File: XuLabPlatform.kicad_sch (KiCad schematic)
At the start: 11 parts, among them J10 Servo, J11 Servo, J12 Thruster, J15 I2C, J16 UART, J4 Servo, J5 Servo, J6 Servo, J7 Servo, J8 Servo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

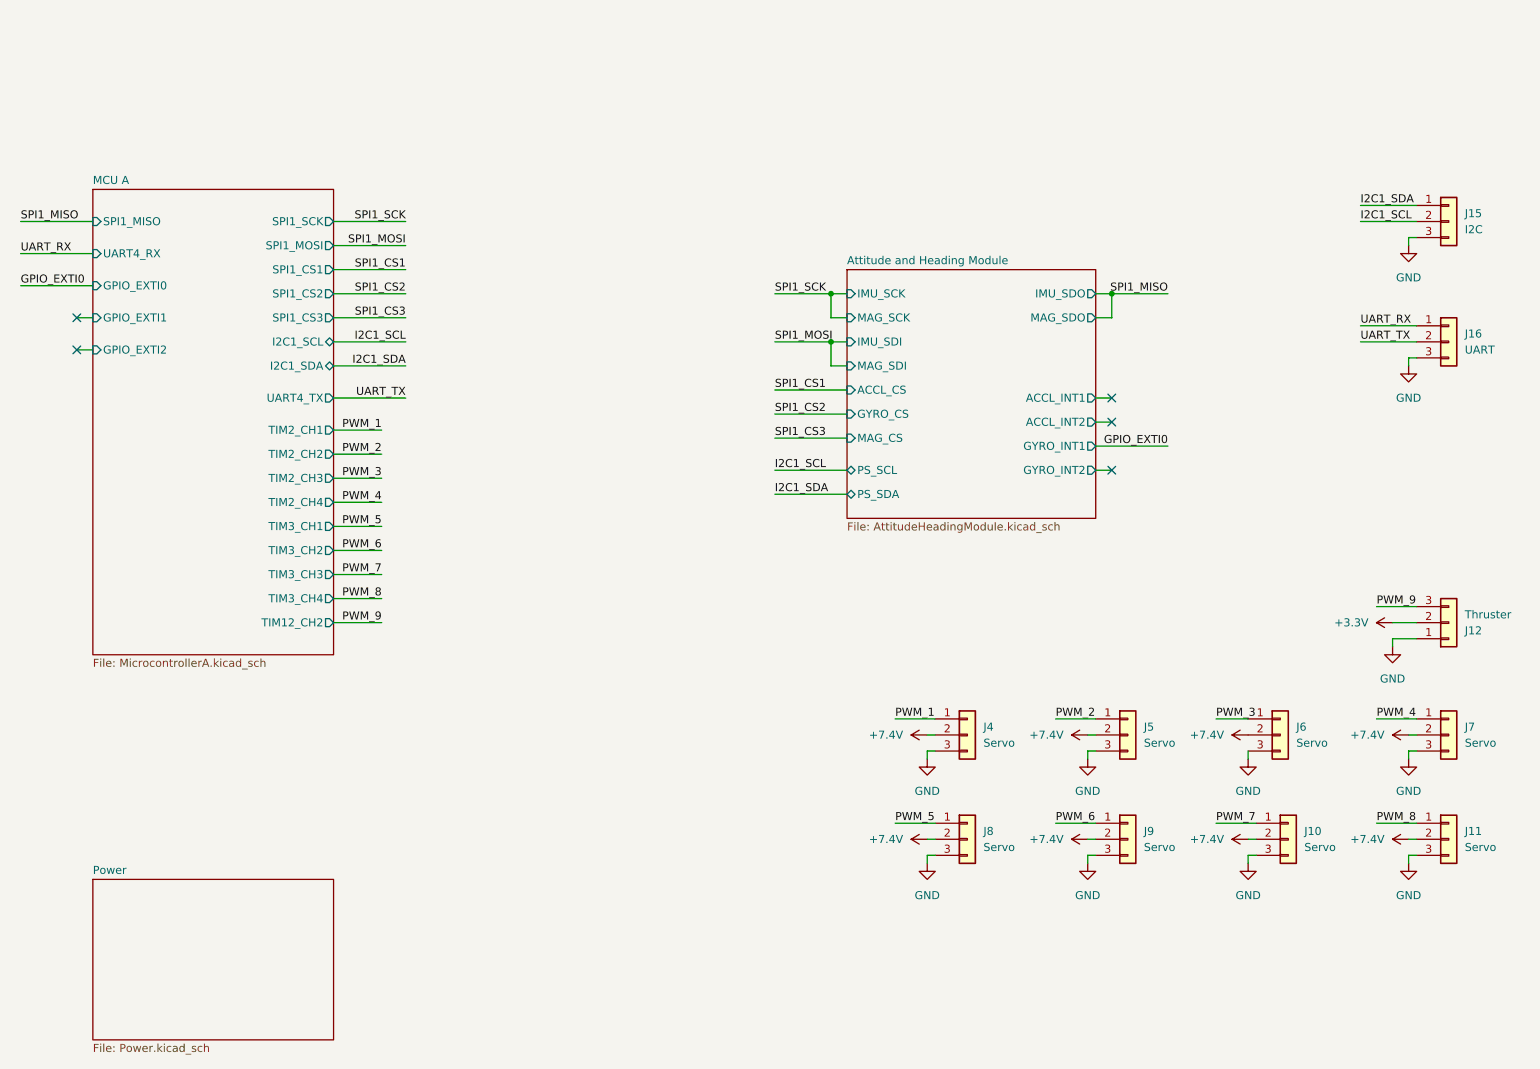
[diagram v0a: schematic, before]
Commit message: Add second SPI pins and connector
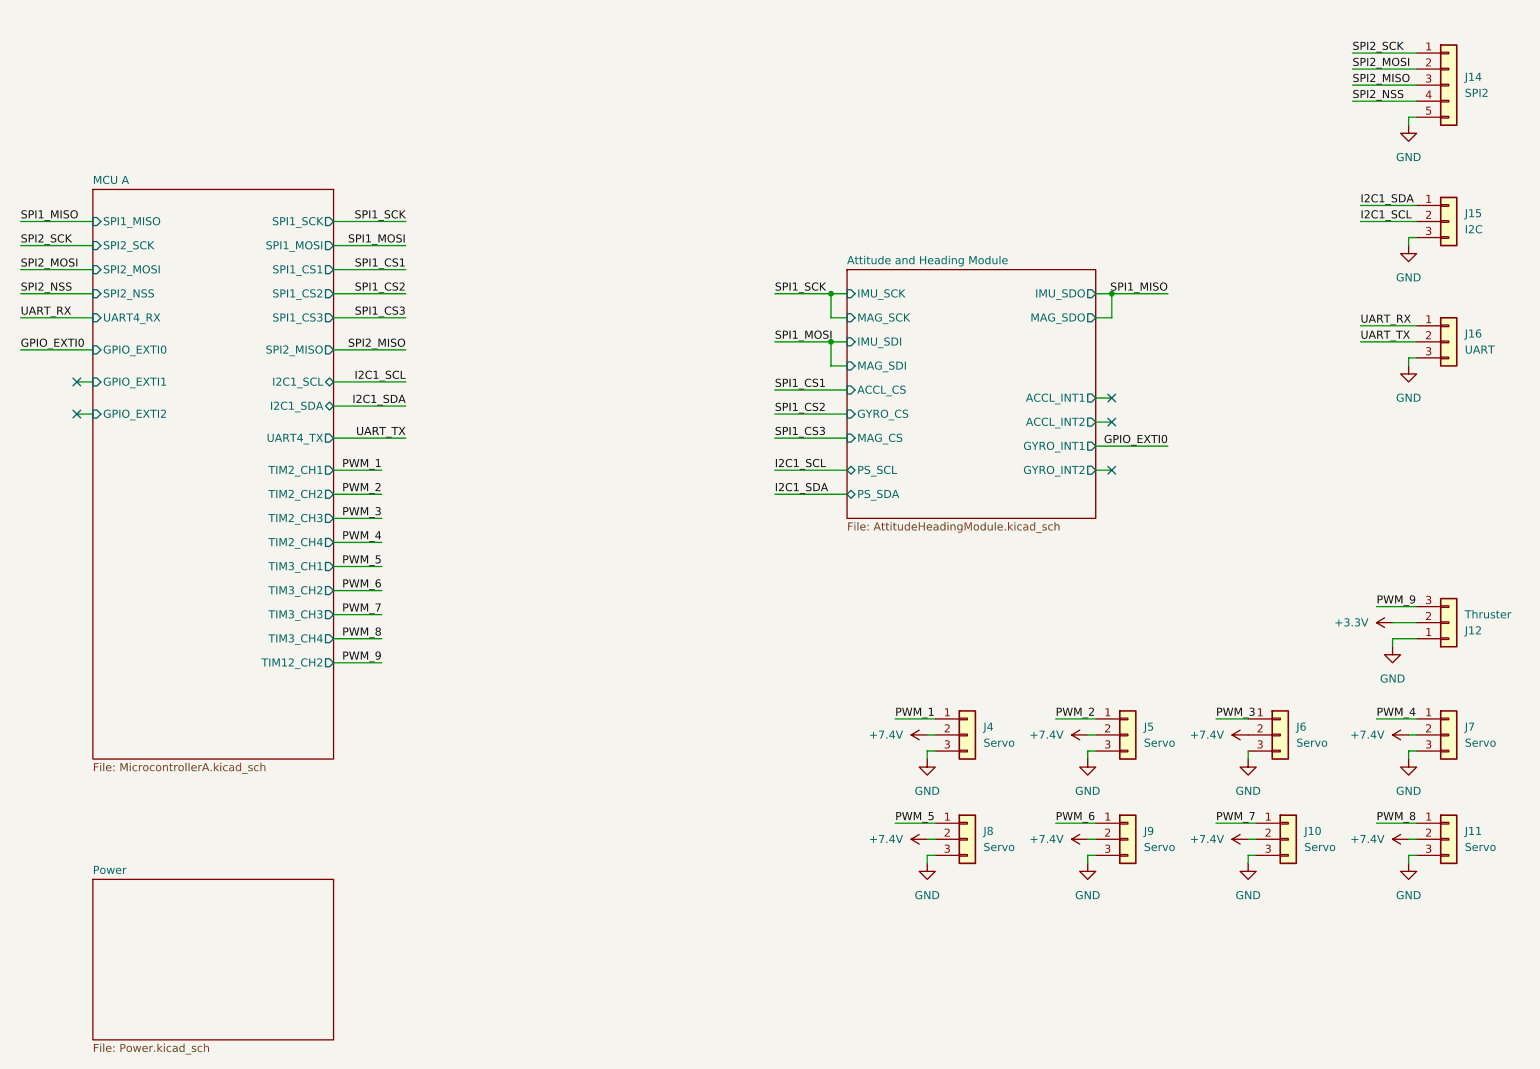
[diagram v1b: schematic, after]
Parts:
- added J14: SPI2, Connector_Molex:Molex_PicoBlade_53048-0510_1x05_P1.25mm_Horizontal, symbol Connector_Generic:Conn_01x05
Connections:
- net GND: now also J14.5 (Pin_5)
- new net SPI2_MISO: J14.3 (Pin_3)
- new net SPI2_MOSI: J14.2 (Pin_2)
- new net SPI2_NSS: J14.4 (Pin_4)
- new net SPI2_SCK: J14.1 (Pin_1)
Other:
- sheet MCU A ports: added SPI2_MISO, SPI2_MOSI, SPI2_NSS, SPI2_SCK; removed none

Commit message: Add second UART interface and connector
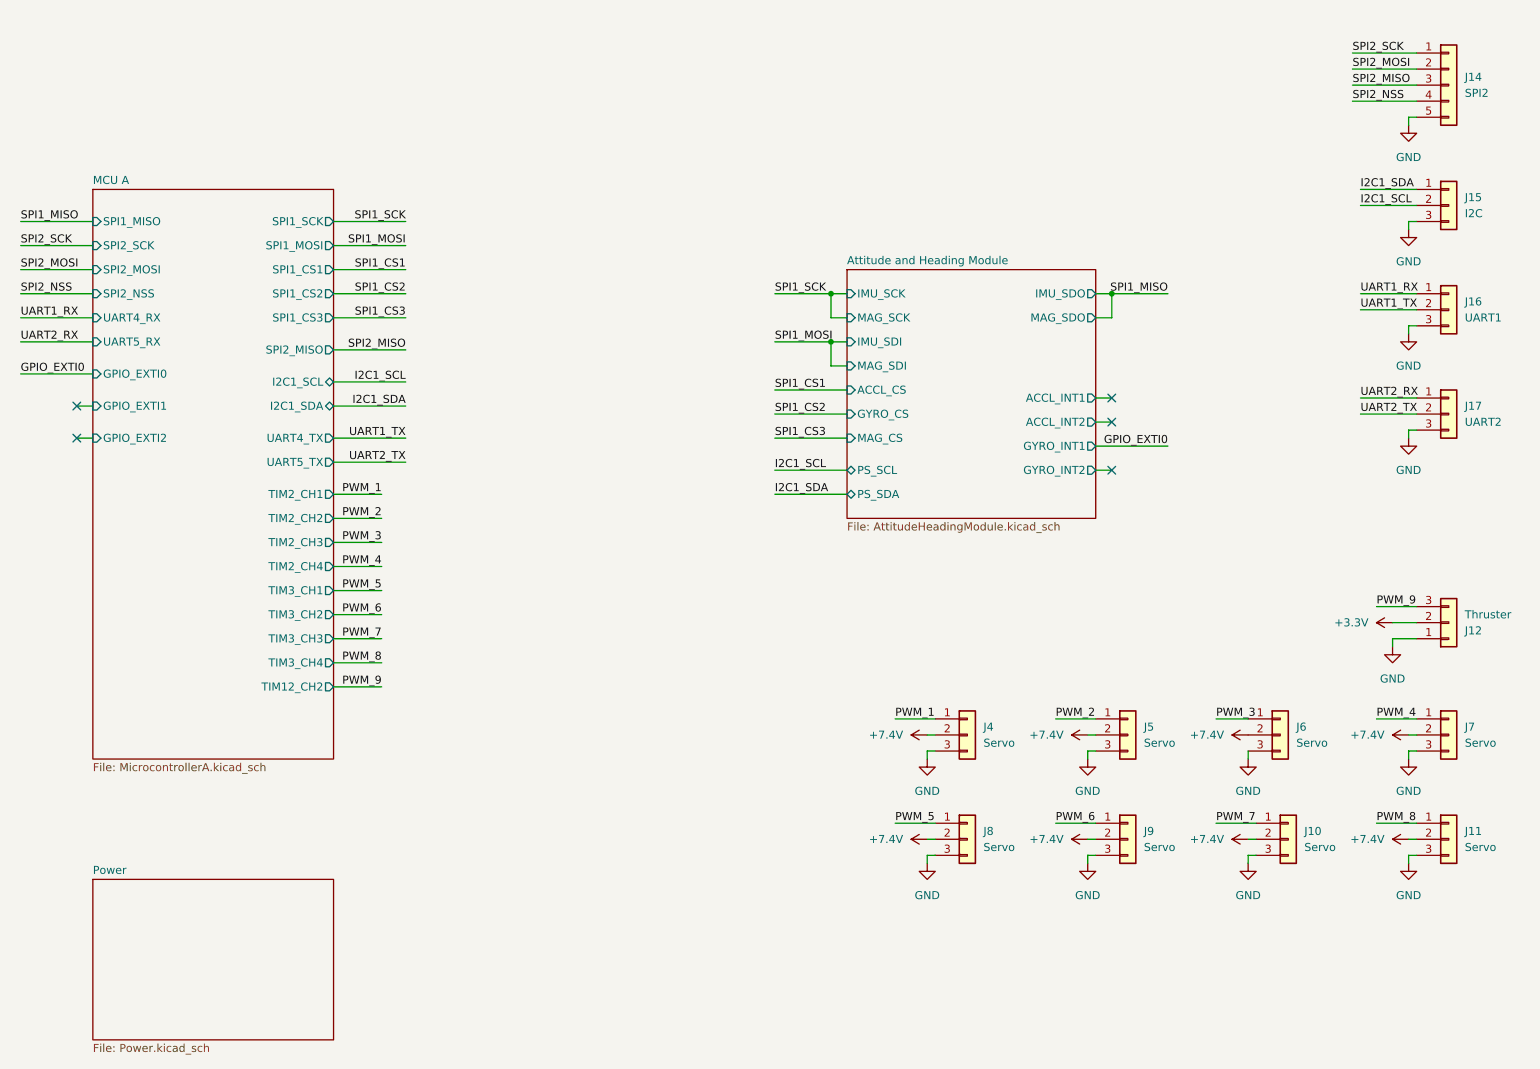
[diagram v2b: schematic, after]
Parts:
- added J17: UART2, Connector_Molex:Molex_PicoBlade_53048-0310_1x03_P1.25mm_Horizontal, symbol Connector_Generic:Conn_01x03
- J16: value UART -> UART1
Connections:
- net GND: now also J17.3 (Pin_3)
- net UART_RX renamed UART1_RX
- net UART_TX renamed UART1_TX
- new net UART2_RX: J17.1 (Pin_1)
- new net UART2_TX: J17.2 (Pin_2)
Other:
- sheet MCU A ports: added UART5_RX, UART5_TX; removed none
- moved on the sheet: J15, J16

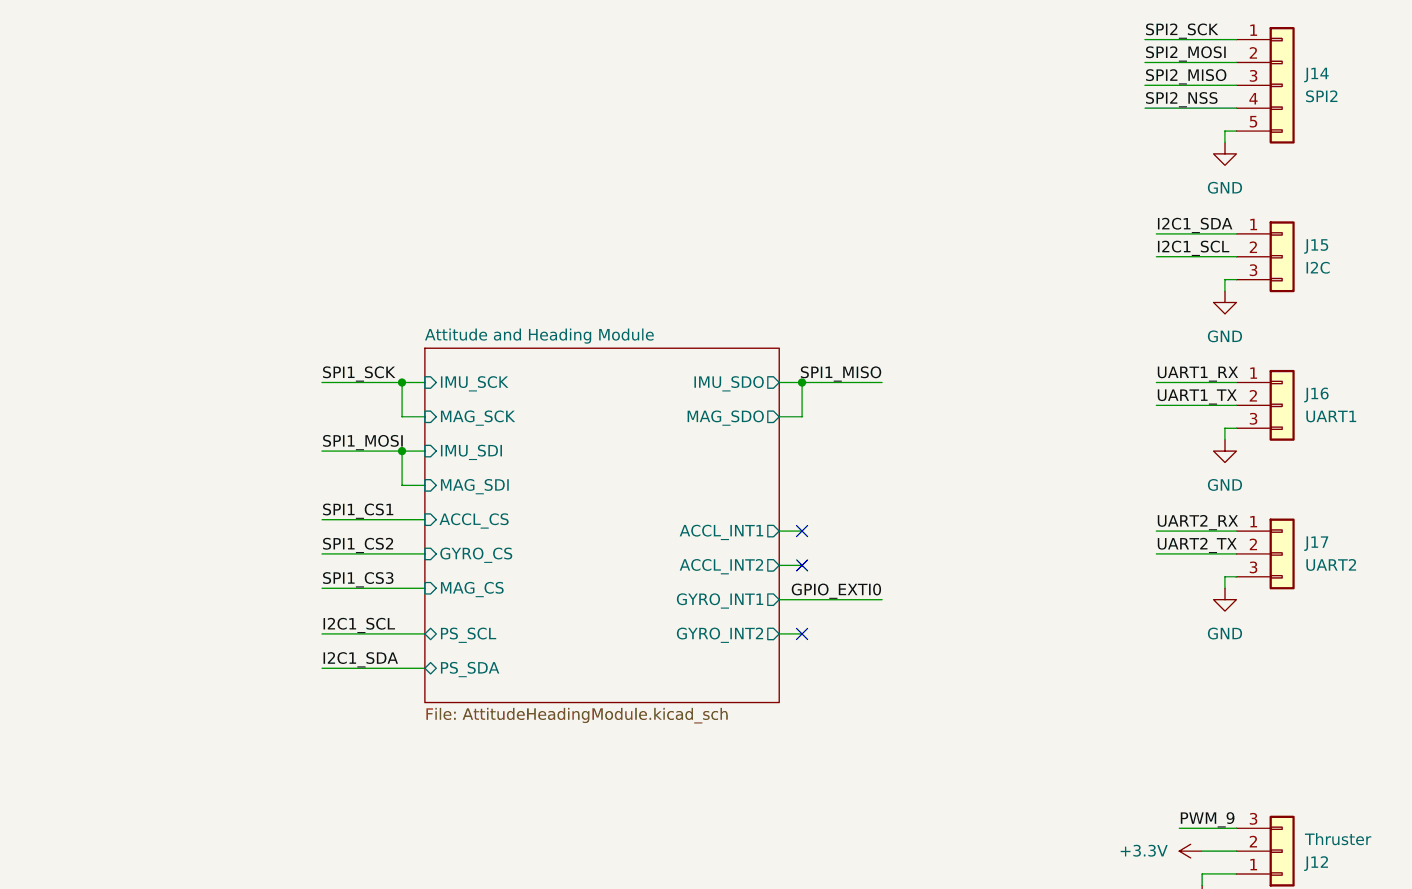
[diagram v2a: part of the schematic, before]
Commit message: Add second I2C connector
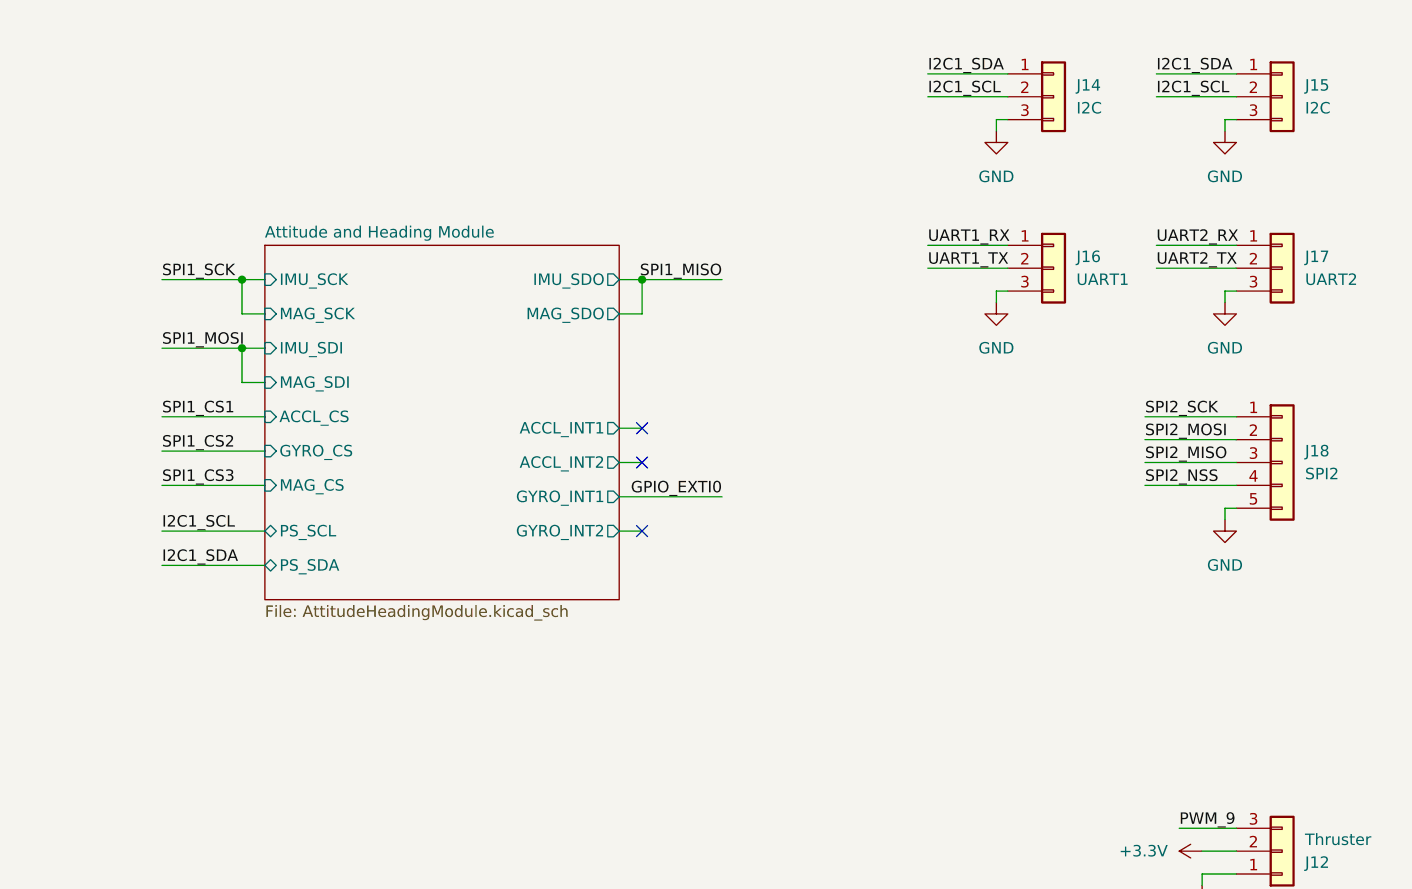
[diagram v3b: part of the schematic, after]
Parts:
- added J15: I2C, Connector_Molex:Molex_PicoBlade_53048-0310_1x03_P1.25mm_Horizontal, symbol Connector_Generic:Conn_01x03
- renumbered J15 to J14, J14 to J18
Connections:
- net GND: now also J15.3 (Pin_3)
- net I2C1_SCL: now also J15.2 (Pin_2)
- net I2C1_SDA: now also J15.1 (Pin_1)
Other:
- moved on the sheet: J14, J16, J17, J18

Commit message: Add second SPI1 connector
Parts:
- added J18: SPI1, Connector_Molex:Molex_PicoBlade_53048-0510_1x05_P1.25mm_Horizontal, symbol Connector_Generic:Conn_01x05
- renumbered J18 to J19
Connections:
- net GND: now also J18.5 (Pin_5)
- net SPI1_MISO: now also J18.3 (Pin_3)
- net SPI1_MOSI: now also J18.2 (Pin_2)
- net SPI1_SCK: now also J18.1 (Pin_1)
- new net SPI1_CS0: J18.4 (Pin_4)
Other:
- sheet MCU A ports: added SPI1_CS0; removed none

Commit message: Connect MCU interrupt pins to sensors
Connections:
- no-connect marks 5 -> 2
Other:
- sheet Attitude and Heading Module ports: added MAG_INT; removed none
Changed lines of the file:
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@@
 	)
 	(no_connect
-		(at 48.26 77.47)
-	)
-	(no_connect
-		(at 48.26 82.55)
-	)
-	(no_connect
-		(at 194.31 64.77)
-	)
-	(no_connect
 		(at 194.31 68.58)
 	)
@@
 	(wire
 		(pts
-			(xy 48.26 77.47) (xy 50.8 77.47)
-		)
-		(stroke
-			(width 0)
-			(type default)
-		)
-	)
-	(wire
-		(pts
 			(xy 233.68 30.48) (xy 233.68 31.75)
 		)
@@
 	(wire
 		(pts
+			(xy 191.77 80.01) (xy 203.2 80.01)
+		)
+		(stroke
+			(width 0)
+			(type default)
+		)
+	)
+	(wire
+		(pts
 			(xy 184.15 148.59) (xy 182.88 148.59)
 		)
@@
 	(wire
 		(pts
+			(xy 39.37 76.2) (xy 50.8 76.2)
+		)
+		(stroke
+			(width 0)
+			(type default)
+		)
+	)
+	(wire
+		(pts
 			(xy 140.97 71.12) (xy 152.4 71.12)
 		)
@@
 	(wire
 		(pts
-			(xy 191.77 64.77) (xy 194.31 64.77)
+			(xy 191.77 64.77) (xy 203.2 64.77)
 		)
 		(stroke
@@
 	(wire
 		(pts
-			(xy 48.26 82.55) (xy 50.8 82.55)
+			(xy 88.9 48.26) (xy 100.33 48.26)
 		)
 		(stroke
@@
 	(wire
 		(pts
-			(xy 88.9 48.26) (xy 100.33 48.26)
+			(xy 88.9 55.88) (xy 100.33 55.88)
 		)
 		(stroke
@@
 	(wire
 		(pts
-			(xy 88.9 55.88) (xy 100.33 55.88)
+			(xy 39.37 80.01) (xy 50.8 80.01)
 		)
 		(stroke
@@
 		)
 	)
+	(label "GPIO_EXTI2"
+		(at 39.37 80.01 0)
+		(effects
+			(font
+				(size 1.27 1.27)
+			)
+			(justify left bottom)
+		)
+	)
 	(label "UART1_TX"
 		(at 100.33 86.36 180)
@@
 		)
 	)
+	(label "GPIO_EXTI1"
+		(at 39.37 76.2 0)
+		(effects
+			(font
+				(size 1.27 1.27)
+			)
+			(justify left bottom)
+		)
+	)
 	(label "SPI2_SCK"
 		(at 250.19 63.5 0)
@@
 		)
 	)
+	(label "GPIO_EXTI2"
+		(at 203.2 80.01 180)
+		(effects
+			(font
+				(size 1.27 1.27)
+			)
+			(justify right bottom)
+		)
+	)
 	(label "UART2_TX"
 		(at 251.46 46.99 0)
@@
 		)
 	)
+	(label "GPIO_EXTI0"
+		(at 203.2 64.77 180)
+		(effects
+			(font
+				(size 1.27 1.27)
+			)
+			(justify right bottom)
+		)
+	)
 	(label "I2C1_SDA"
 		(at 140.97 80.01 0)
@@
 		)
 	)
-	(label "GPIO_EXTI0"
+	(label "GPIO_EXTI1"
 		(at 203.2 72.39 180)
 		(effects
@@
 		)
 		(pin "GPIO_EXTI1" input
-			(at 50.8 77.47 180)
+			(at 50.8 76.2 180)
 			(effects
 				(font
@@
 		)
 		(pin "GPIO_EXTI2" input
-			(at 50.8 82.55 180)
+			(at 50.8 80.01 180)
 			(effects
 				(font
@@
 			(effects
 				(font
+					(size 1.27 1.27)
+				)
+				(justify right)
+			)
+		)
+		(pin "MAG_INT" input
+			(at 191.77 80.01 0)
+			(effects
+				(font
